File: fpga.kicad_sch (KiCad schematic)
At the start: 57 parts, among them J7 2X05, Q6 2N7002, U11 LIFCL-40-9BG256C, U17 SC18IS602BIPW, U18 W25Q32JVSSIQ, Y2 OSC40M-3.3_S5

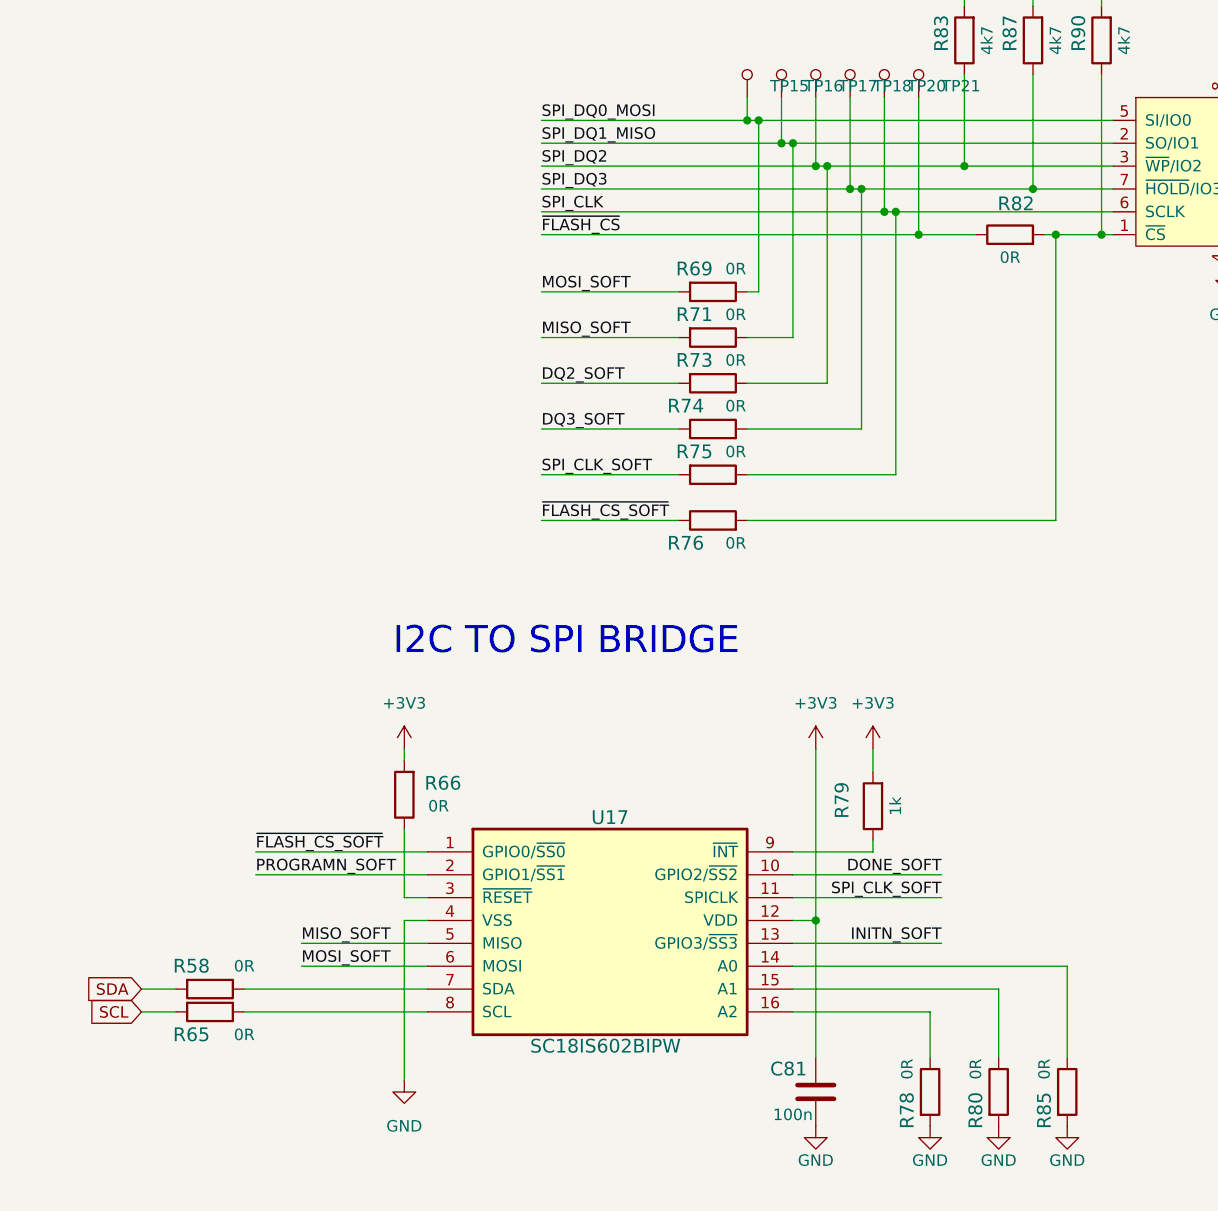
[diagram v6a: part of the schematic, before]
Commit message: Routed flash memory
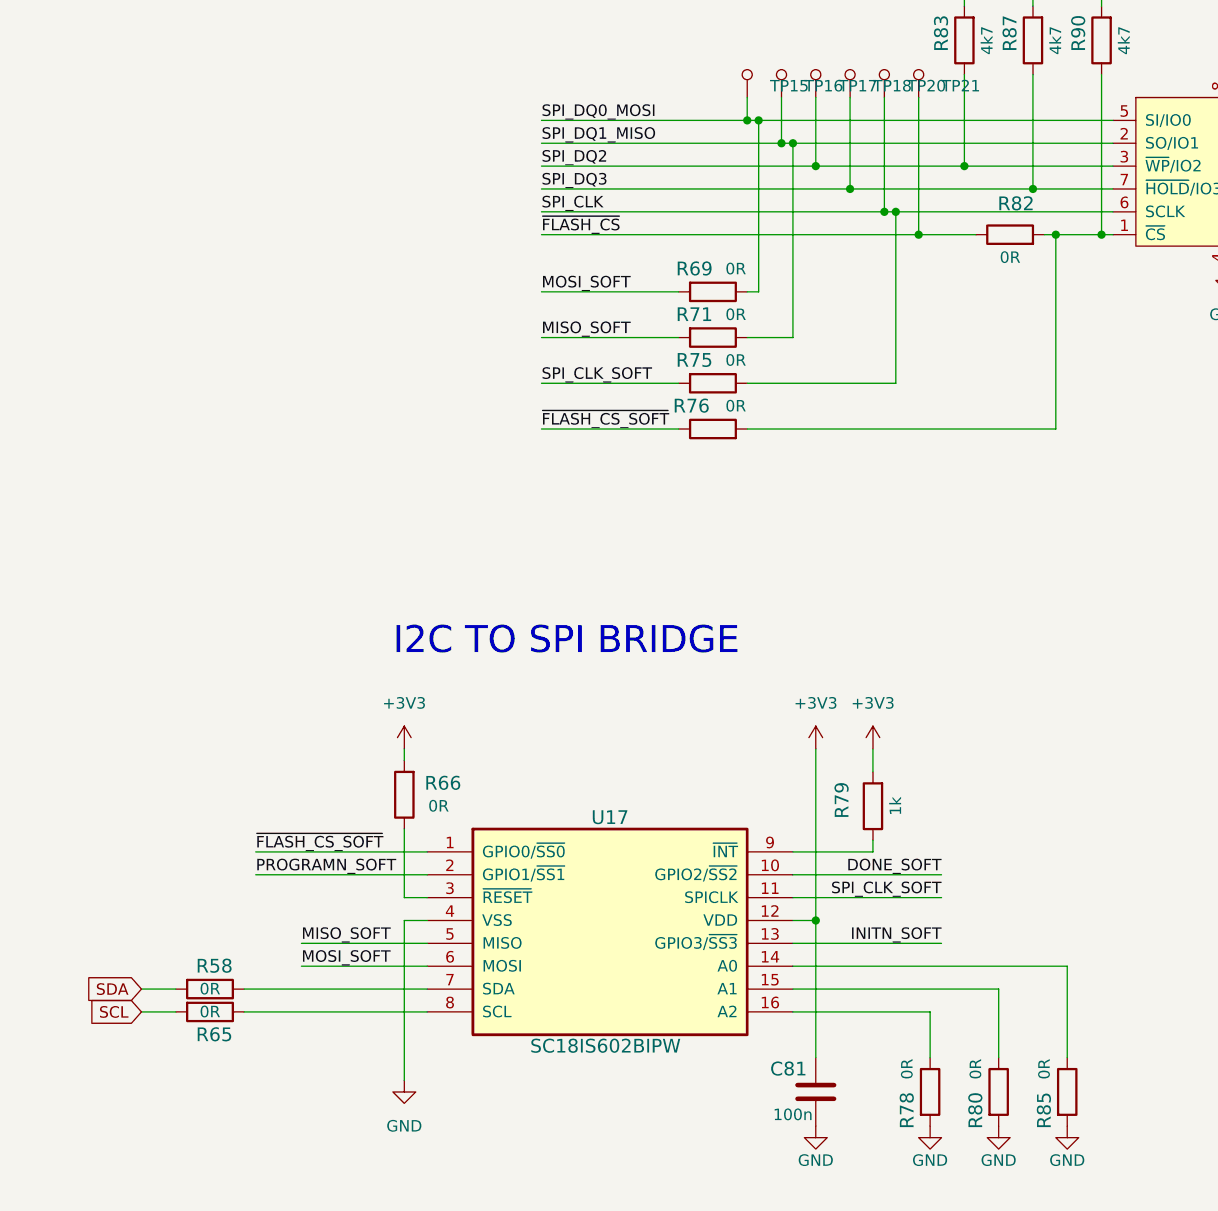
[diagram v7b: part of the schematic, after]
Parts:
- removed R73, R74: R_0R_0402, crosslink-nx-video-converter-footprints:0402-res, symbol crosslink-nx-video-converter:R_0R_0402
- R58, R65: footprint crosslink-nx-video-converter-footprints:0402-res -> antmicro-footprints:0603-res; symbol crosslink-nx-video-converter:R_0R_0402 -> antmicroResistors0603:R_0R_0603; MPN ERJ2GE0R00X -> CR0603-J/-000ELF; Manufacturer PANASONIC -> BOURNS
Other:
- moved on the sheet: R75, R76

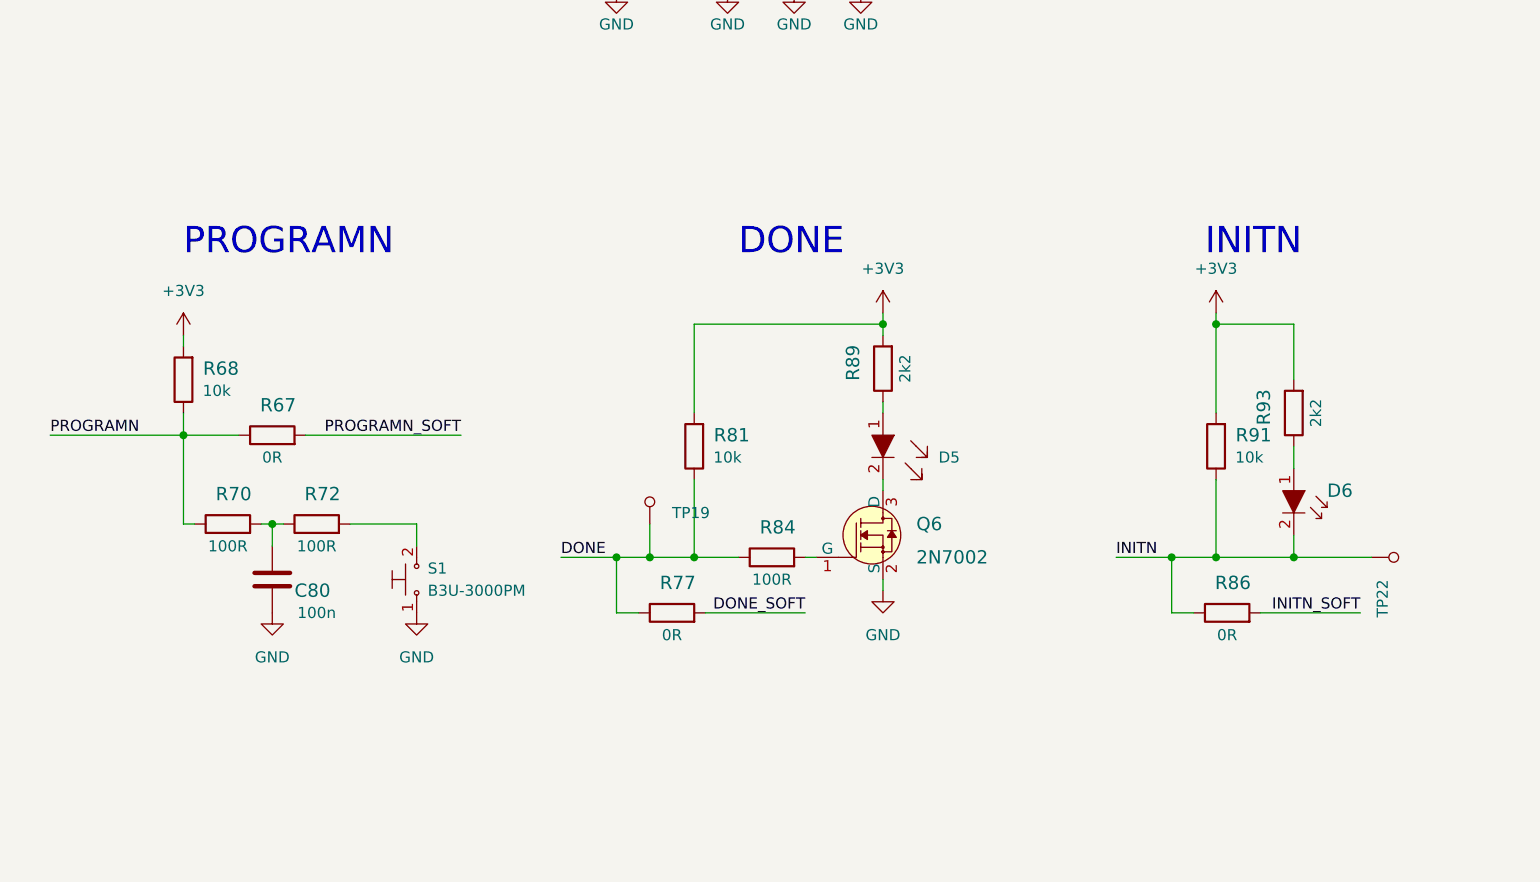
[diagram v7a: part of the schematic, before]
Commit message: Added FT230XQ-R for USB connectivity
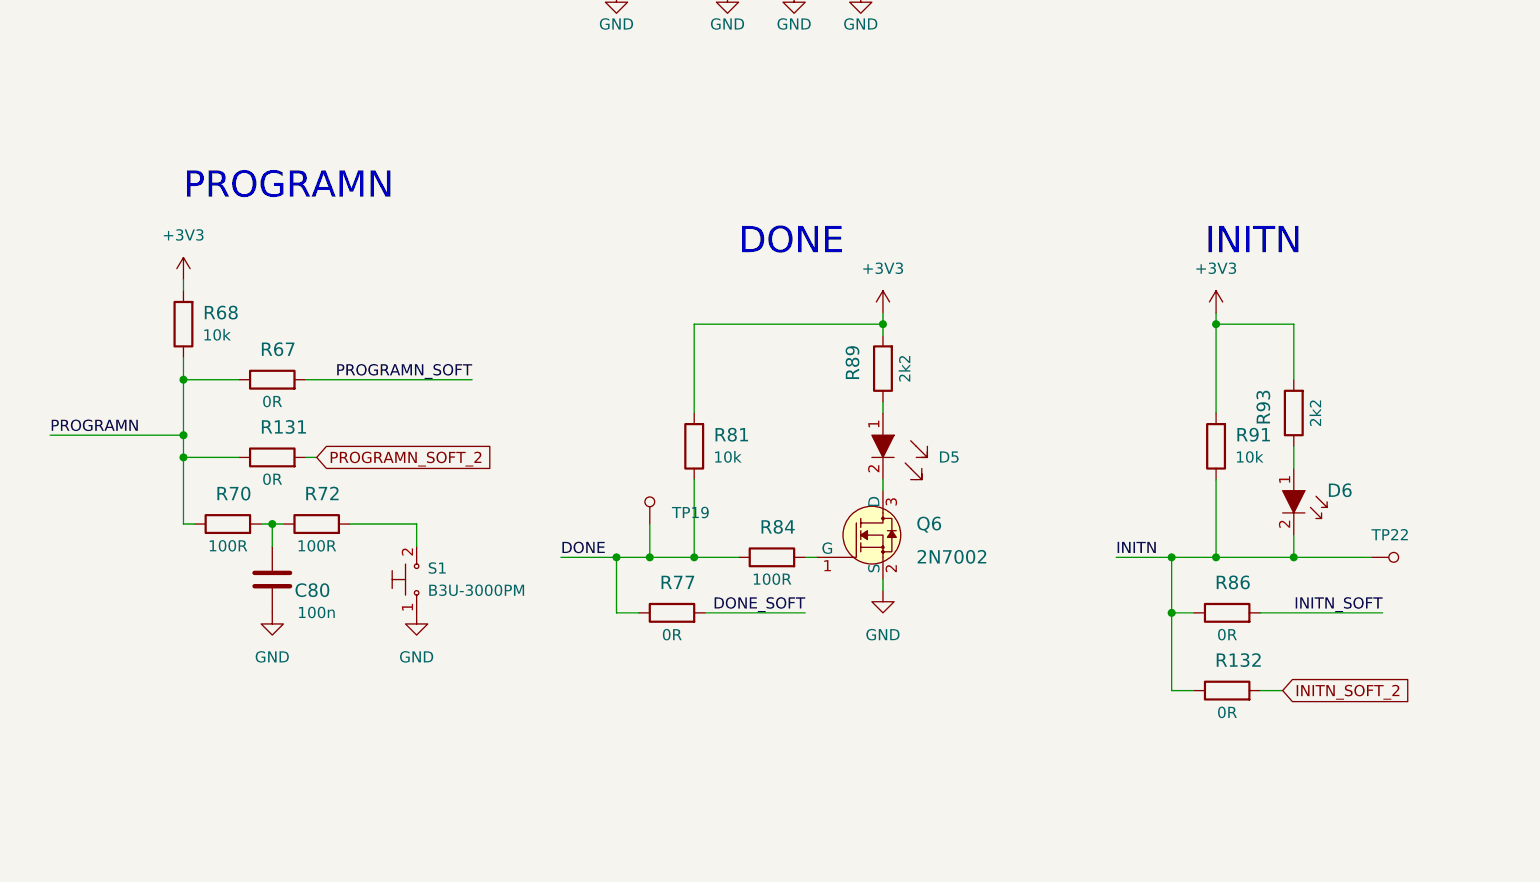
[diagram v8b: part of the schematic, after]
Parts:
- added R131, R132: R_0R_0402, crosslink-nx-video-converter-footprints:0402-res, symbol crosslink-nx-video-converter:R_0R_0402
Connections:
- net INITN: now also R132.1
- net PROGRAMN: now also R131.1
- new net INITN_SOFT_2: R132.2
- new net PROGRAMN_SOFT_2: R131.2
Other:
- moved on the sheet: R67, R68
